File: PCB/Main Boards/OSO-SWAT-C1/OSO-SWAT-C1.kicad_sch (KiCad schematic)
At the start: 35 parts, among them J1 OSO_SWD, J2 FH19C-9S-0.5SH_10_, Q1 Q_Photo_NPN, Q2 Q_NMOS_GSD, U1 ATSAML22J18A-MUT, U2 MIC5365-3.3YC5-TR, X1 Crystal

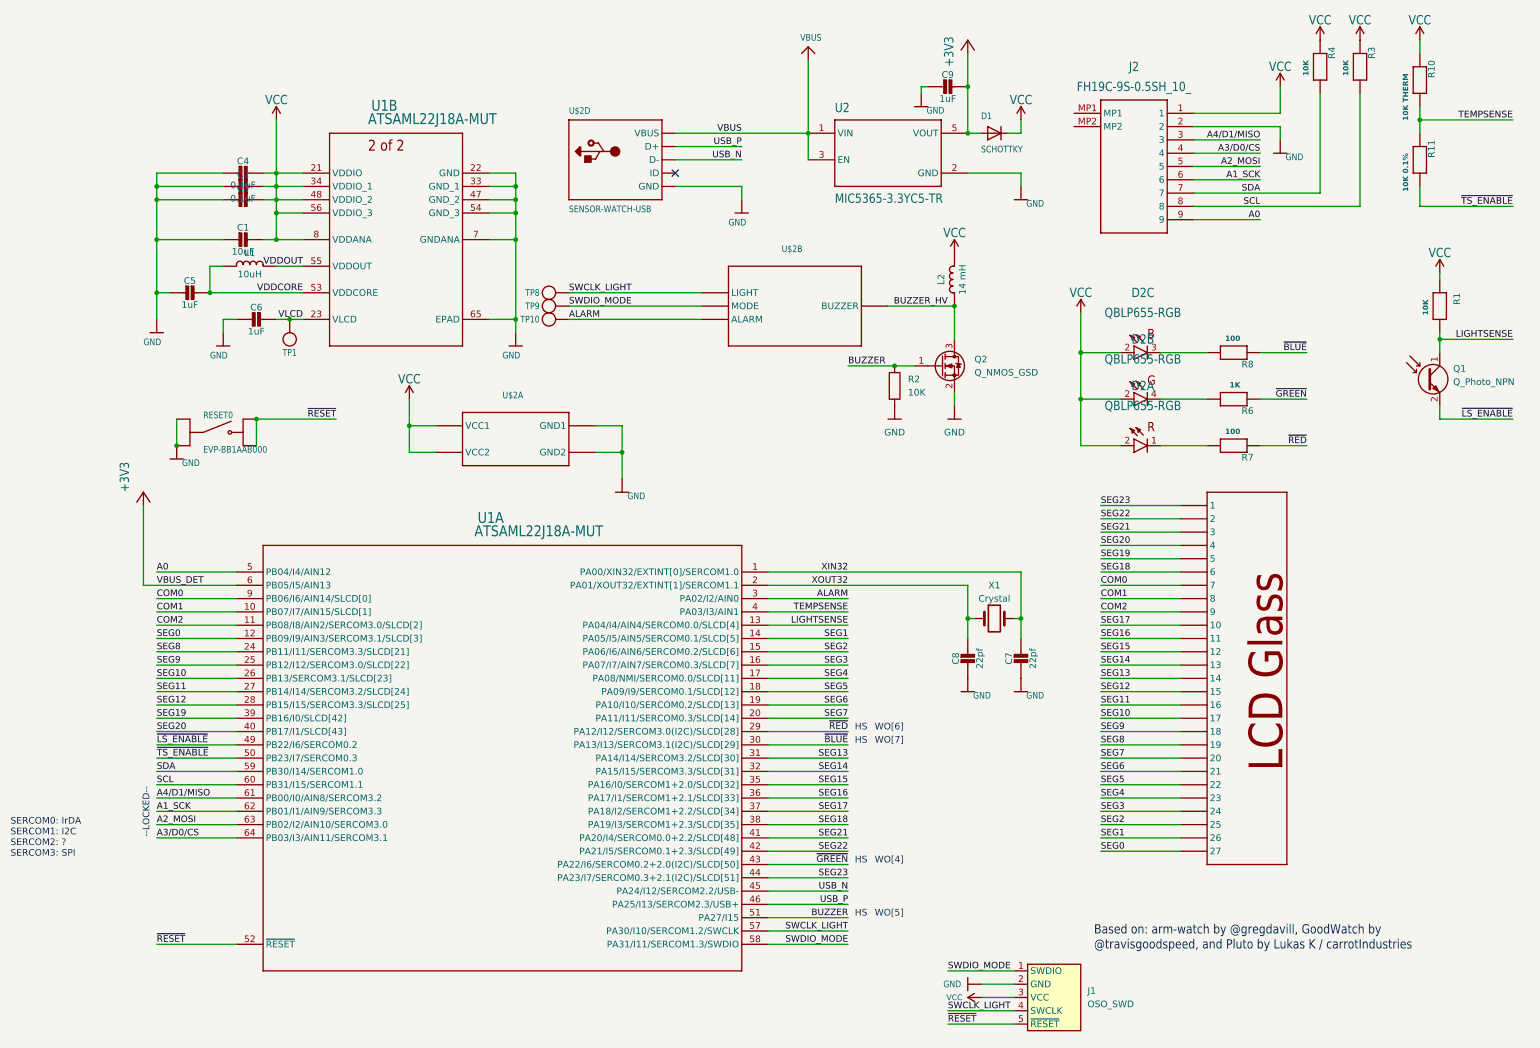
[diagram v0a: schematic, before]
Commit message: break swd pins into separate footprints
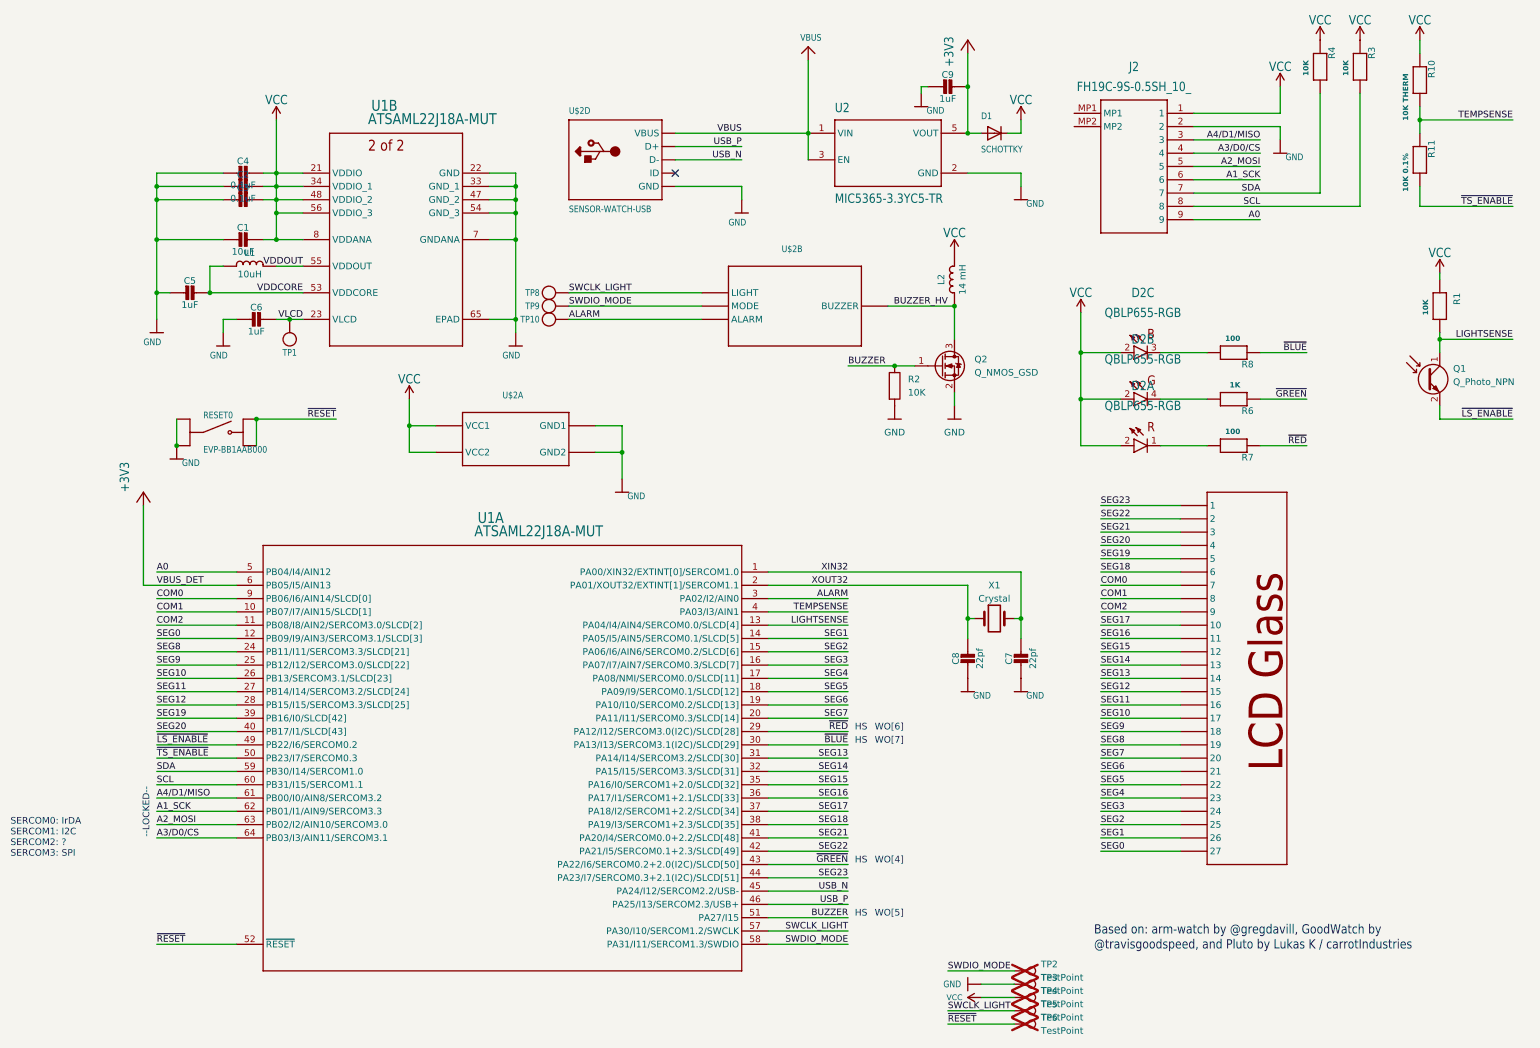
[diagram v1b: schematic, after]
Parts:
- removed J1: OSO_SWD, OSO-SWD:OSO_SWD_2x3, symbol OSO-SWD:OSO_SWD
- added TP2, TP3, TP4, TP5, TP6: TestPoint, TestPoint:TestPoint_Pad_D1.5mm, symbol Connector:TestPoint
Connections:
- net GND: now also TP3.1
- net SWCLK_LIGHT: now also TP5.1
- net SWDIO_MODE: now also TP2.1
- net VCC: now also TP4.1
- net ~{RESET}: now also TP6.1
